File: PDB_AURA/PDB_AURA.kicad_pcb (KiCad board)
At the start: 4 copper layers, 50 x 50 mm, 83 parts, among them J100 XT30PW-M, J300 XT30PW-F, J301 XT30PW-F, J302 532617012, J303 XT30PW-F, J304 XT30PW-F, Q100 CSD18540Q5B, Q200 CSD18540Q5B, Q201 CSD18510Q5B, Q300 HSK10N06, Q301 HSK10N06, U100 LM74700, U200 LM25145RGYR, U300 LTV-217-B-G, U301 LTV-217-B-G, U302 INA219AIDCNR

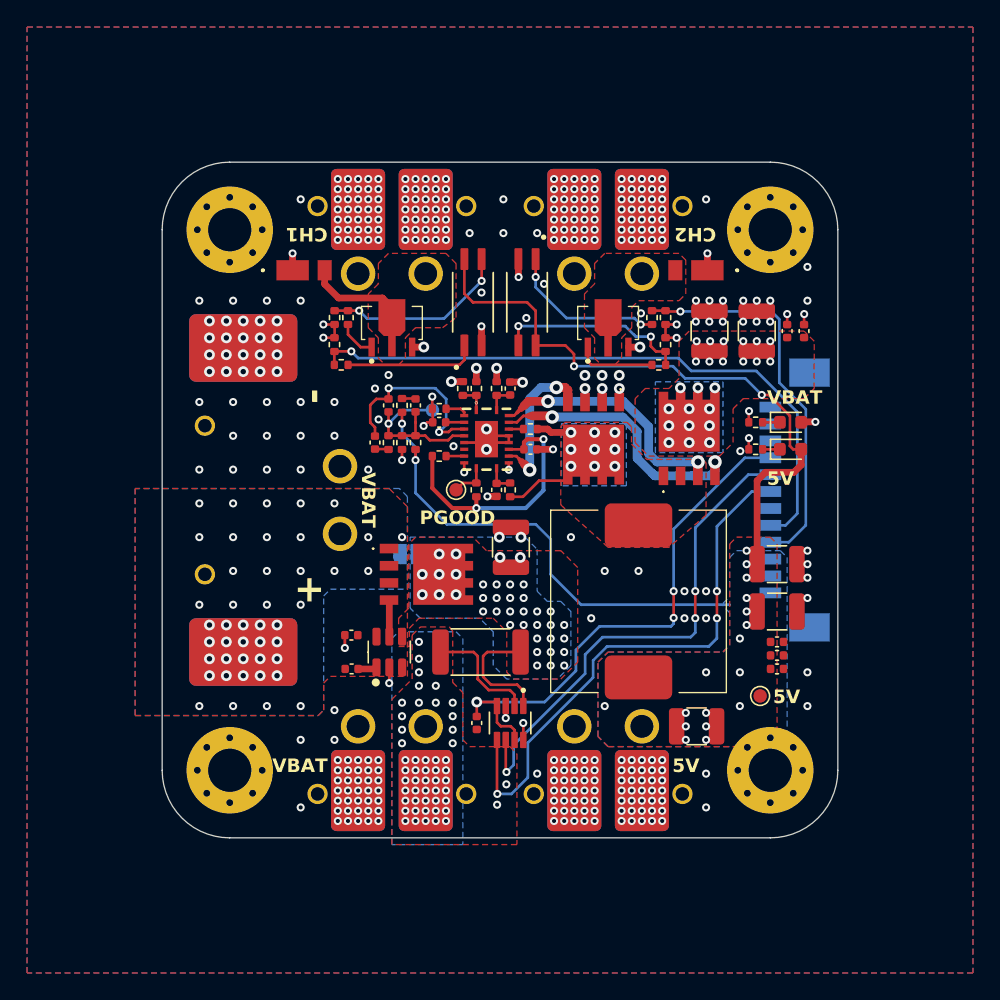
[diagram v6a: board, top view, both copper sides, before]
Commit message: Re Routing some of the power board
Connectors had positive and negative the wrong way around, and some of the routing did not look good.
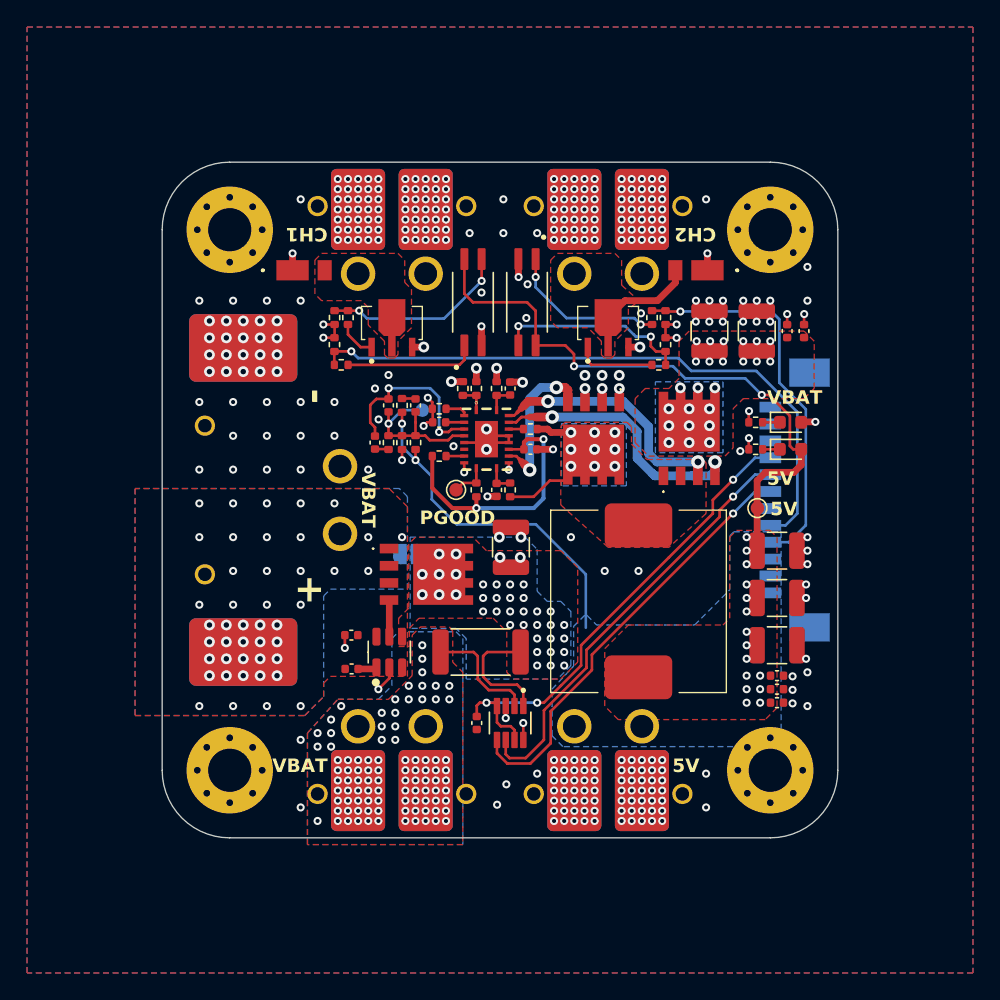
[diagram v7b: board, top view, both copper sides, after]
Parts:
- R101: value 4k7 -> 2k2
- moved TP200 13.9 mm to (94.0, 75.6)
- moved C205 8.45 mm to (95.5, 85.8)
- moved J309 5.00 mm to (80.5, 96.5)
- moved J310 5.00 mm to (85.5, 96.5)
- moved J311 5.00 mm to (64.5, 96.5)
- moved J312 5.00 mm to (69.5, 96.5)
- moved C202 2.50 mm to (95.5, 88.0)
- moved C203 2.50 mm to (95.5, 89.0)
- moved C215 2.50 mm to (95.5, 90.0)
- moved C204 1.00 mm to (95.5, 82.2)
- moved C216 1.00 mm to (95.5, 78.8)
- moved TP201 0.75 mm to (69.2, 68.3)
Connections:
- J300 pad 1: +BATT_FILT -> /300_Connectors/VBAT_CH1
- J300 pad 2: /300_Connectors/VBAT_CH1 -> +BATT_FILT
- J301 pad 1: +BATT_FILT -> /300_Connectors/VBAT_CH2
- J301 pad 2: /300_Connectors/VBAT_CH2 -> +BATT_FILT
- J303 pad 1: +BATT_FILT -> GND
- J303 pad 2: GND -> +BATT_FILT
- J303 pad 3: +BATT_FILT -> GND
- J303 pad 4: GND -> +BATT_FILT
- J304 pad 1: +5V -> GND
- J304 pad 2: GND -> +5V
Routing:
- net +5V: track 82.0 -> 72.5 mm, vias 18 -> 19
- net SCL: track 40.6 -> 31.9 mm, vias 3 -> 1
- net /300_Connectors/VBAT_CH2: track 0.00 -> 6.97 mm
- net /300_Connectors/VBAT_CH1: track 6.71 -> 0.00 mm
- net SDA: track 37.2 -> 31.8 mm, vias 3 -> 1
- net +3V3: track 40.0 -> 35.6 mm
- net GND: track 31.6 -> 32.4 mm, vias 268 -> 263
- net /200_Buck_Regulator/5V_FB: track 13.1 -> 12.3 mm
- net /200_Buck_Regulator/COMP_FB_C: track 14.0 -> 13.3 mm
- net +BATT_FILT: vias 184 -> 194

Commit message: First review for PDB.
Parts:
- added TP100: TestPoint, TestPoint:TestPoint_Pad_D1.0mm, F.Cu at (67.2, 76.0)
- added TP101: TestPoint, TestPoint:TestPoint_Pad_D1.0mm, F.Cu at (70.8, 89.2)
- moved TP200 2.69 mm to (94.8, 73.0)
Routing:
- net SCL: track 31.9 -> 36.2 mm
- net SDA: track 31.8 -> 35.6 mm
- net +3V3: track 35.6 -> 39.3 mm
- net /300_Connectors/VGS_CH2: track 14.5 -> 16.0 mm
- net /300_Connectors/MSFT_2_R: track 11.8 -> 13.0 mm
- net GND: track 32.4 -> 31.4 mm, vias 263 -> 276
- net +BATT: vias 44 -> 43
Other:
- board text added: "FILT"
